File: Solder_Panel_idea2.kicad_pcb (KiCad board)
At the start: 2 copper layers, 152.5 x 101.5 mm, 45 parts, among them SW1 SW_SPDT_1825232-1, U1 SA555P, U2 SA555P

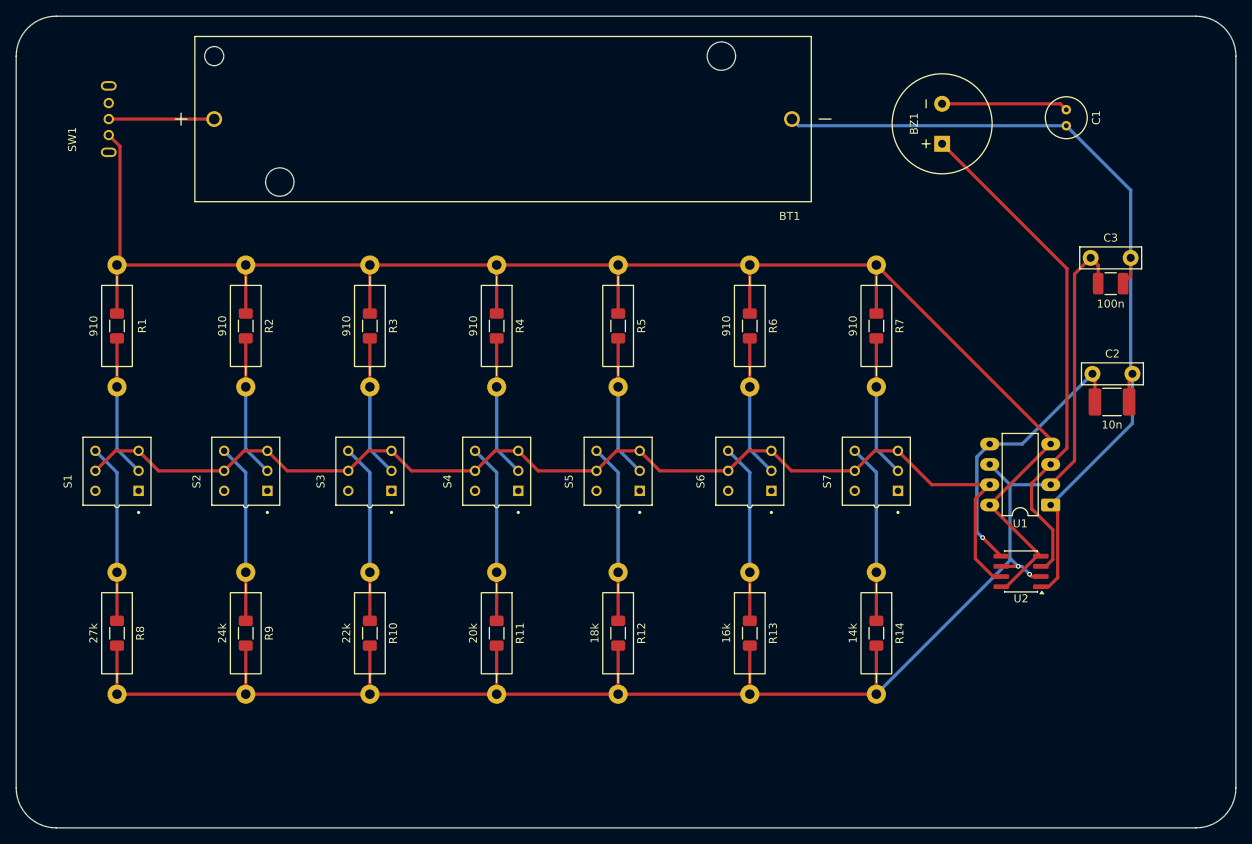
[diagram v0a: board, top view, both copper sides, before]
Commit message: layout changes, art, add 8th note
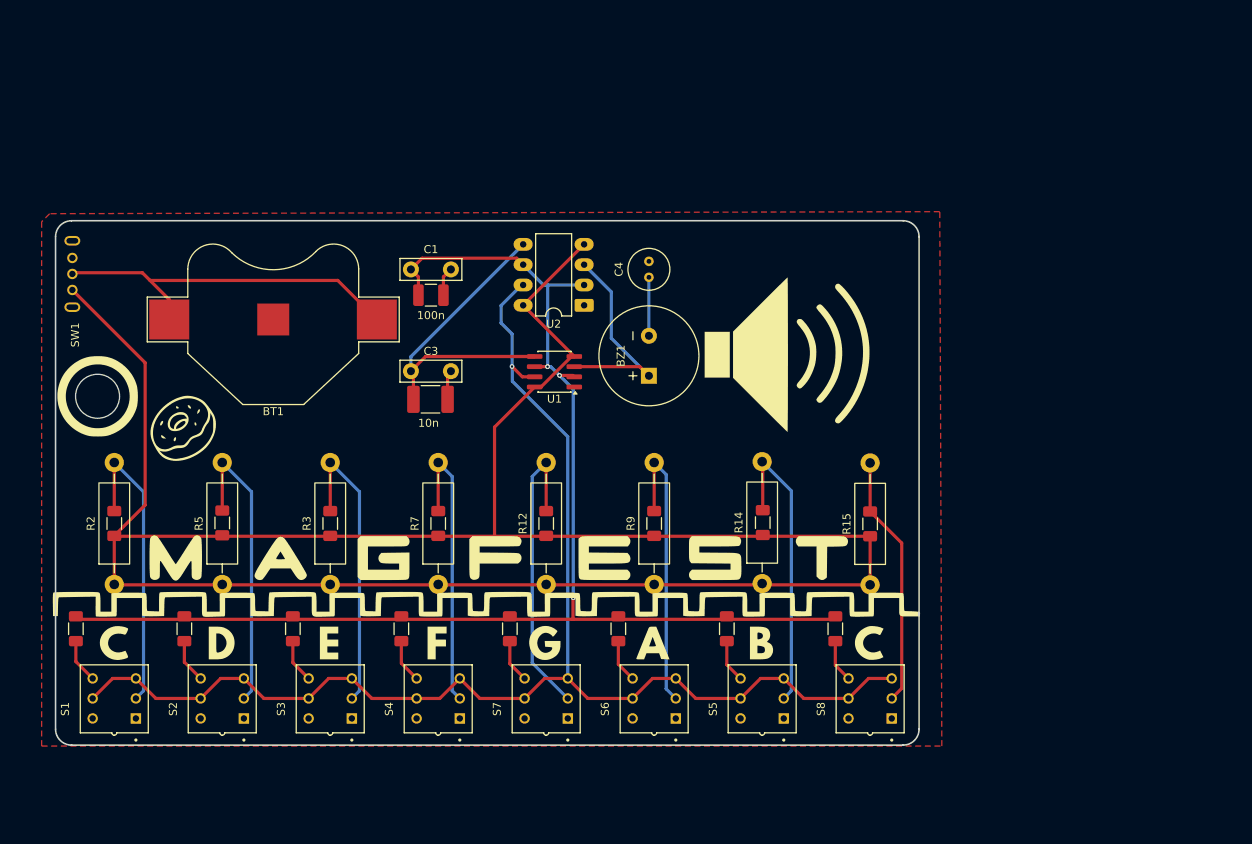
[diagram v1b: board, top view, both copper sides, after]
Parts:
- removed the R13 at (108.5, 85.2)
- removed the R16 at (45.5, 54.4)
- removed the R17 at (61.0, 54.4)
- removed the R18 at (76.9, 54.4)
- removed the R19 at (92.1, 54.4)
- removed the R20 at (108.5, 54.4)
- removed the R21 at (124.3, 54.4)
- added R13: 910, Resistor_SMD:R_1206_3216Metric_Pad1.30x1.75mm_HandSolder, F.Cu at (110.1, 79.0)
- added R13: 910, Resistor_SMD:R_1206_3216Metric_Pad1.30x1.75mm_HandSolder, F.Cu at (123.6, 79.1)
- added R22: 13.2k, Resistor_SMD:R_1206_3216Metric_Pad1.30x1.75mm_HandSolder, F.Cu at (119.2, 92.2)
- added REF**: MountingHole_5.5mm, MountingHole:MountingHole_5.5mm, F.Cu at (27.0, 63.2)
- added S8: C5379898, TL2201EEYA:SW_TL2201EEYA, F.Cu at (123.6, 101.0)
- BT1: footprint 1043:BAT_1043 -> Battery:BatteryHolder_Multicomp_BC-2001_1x2032
- R1, R4, R6: footprint Resistor_THT:R_Axial_DIN0411_L9.9mm_D3.6mm_P15.24mm_Horizontal -> Resistor_SMD:R_1206_3216Metric_Pad1.30x1.75mm_HandSolder
- R10: value 22k -> 910; footprint Resistor_THT:R_Axial_DIN0411_L9.9mm_D3.6mm_P15.24mm_Horizontal -> Resistor_SMD:R_1206_3216Metric_Pad1.30x1.75mm_HandSolder
- R11: value 20k -> 910; footprint Resistor_THT:R_Axial_DIN0411_L9.9mm_D3.6mm_P15.24mm_Horizontal -> Resistor_SMD:R_1206_3216Metric_Pad1.30x1.75mm_HandSolder
- R12: value 18k -> 910
- R14: value 14k -> 910
- R15: footprint Resistor_SMD:R_1206_3216Metric_Pad1.30x1.75mm_HandSolder -> Resistor_THT:R_Axial_DIN0411_L9.9mm_D3.6mm_P15.24mm_Horizontal
- R8: value 27k -> 910; footprint Resistor_THT:R_Axial_DIN0411_L9.9mm_D3.6mm_P15.24mm_Horizontal -> Resistor_SMD:R_1206_3216Metric_Pad1.30x1.75mm_HandSolder
- R9: value 24k -> 910
- S1, S2, S3, S4, S6: value TL2201EEYA -> C5379898; footprint TL2201EEYA:SW_TL2201EEYA -> sao:SW_5.8WSPT
- S5: renamed from S7; value TL2201EEYA -> C5379898
- S7: renamed from S5; value TL2201EEYA -> C5379898; footprint TL2201EEYA:SW_TL2201EEYA -> sao:SW_5.8WSPT
- U1: renamed from U2; value SA555P -> ICM7555IBAZ-T
- U2: renamed from U1; value SA555P -> ICM7555IBAZ-T
- moved R15 99.5 mm to (123.6, 86.8), turned to 90 degrees
- moved C5 85.2 mm to (68.6, 63.6)
- moved C3 85.2 mm to (66.2, 60.0)
- moved C1 85.0 mm to (66.2, 47.3)
- moved C2 85.0 mm to (68.7, 50.5)
- moved R7 67.8 mm to (69.6, 86.7), turned to 90 degrees
- moved R5 63.6 mm to (42.6, 86.7), turned to 90 degrees
- moved U1 63.4 mm to (84.1, 60.1)
- moved U2 63.4 mm to (87.8, 51.8)
- moved R6 61.6 mm to (56.1, 79.1), turned to 90 degrees
- moved C4 56.2 mm to (95.9, 48.3), turned to 90 degrees
- moved R9 51.1 mm to (96.6, 86.7), turned to 90 degrees
- moved R4 47.1 mm to (42.6, 79.0), turned to 90 degrees
- moved BZ1 46.7 mm to (95.9, 58.1)
- moved R2 43.2 mm to (29.1, 86.7), turned to 90 degrees
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- renumbered C3 to C1, C5 to C2, C2 to C3, C1 to C4, C4 to C5, R22 to R15, R24 to R16, R23 to R17, R26 to R18, R25 to R19, R27 to R20, R28 to R21
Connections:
- R10 pad 1: Net-(R10-Pad1) -> Net-(SW1-C)
- R10 pad 2: Net-(U1-THR) -> Net-(R20-Pad2)
- R11 pad 1: Net-(R11-Pad1) -> Net-(SW1-C)
- R11 pad 2: Net-(U1-THR) -> Net-(R19-Pad2)
- R12 pad 1: Net-(R12-Pad1) -> Net-(SW1-C)
- R12 pad 2: Net-(U1-THR) -> Net-(R19-Pad2)
- R14 pad 1: Net-(R14-Pad1) -> Net-(SW1-C)
- R14 pad 2: Net-(U1-THR) -> Net-(R21-Pad2)
- R15 pad 2: Net-(R1-Pad2) -> (no net)
- R2 pad 2: Net-(R16-Pad2) -> Net-(R1-Pad2)
- R4 pad 2: Net-(R18-Pad2) -> Net-(R16-Pad2)
- R5 pad 2: Net-(R19-Pad2) -> Net-(R16-Pad2)
- R6 pad 2: Net-(R20-Pad2) -> Net-(R17-Pad2)
- R7 pad 2: Net-(R21-Pad2) -> Net-(R18-Pad2)
- R8 pad 1: Net-(R22-Pad1) -> Net-(SW1-C)
- R8 pad 2: Net-(U1-THR) -> Net-(R18-Pad2)
- R9 pad 1: Net-(R23-Pad1) -> Net-(SW1-C)
- R9 pad 2: Net-(U1-THR) -> Net-(R20-Pad2)
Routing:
- net GND: track 109.0 -> 7.61 mm
- net Net-(SW1-C): track 212.1 -> 284.3 mm
- net Net-(U1-THR): track 220.1 -> 170.0 mm, vias 2 -> 3
- net (no net): track 0.00 -> 36.9 mm
- net Net-(BZ1--): track 63.2 -> 27.0 mm
- net Net-(SW1-B): track 13.2 -> 46.4 mm
- net Net-(U1-DIS): track 141.2 -> 172.7 mm, vias 0 -> 1
- net Net-(R19-Pad2): track 17.7 -> 38.1 mm
- net Net-(R21-Pad2): track 17.7 -> 37.6 mm
- net Net-(R17-Pad2): track 17.7 -> 37.5 mm
- net Net-(R1-Pad2): track 17.7 -> 37.5 mm
- net Net-(R16-Pad2): track 17.7 -> 37.4 mm
- net Net-(R20-Pad2): track 17.7 -> 36.7 mm
- net Net-(R18-Pad2): track 17.7 -> 36.7 mm
- net Net-(R14-Pad1): track 22.4 -> 5.37 mm
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- added copper zone on F.Cu, net GND
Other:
- board size 152.5 x 101.5 mm -> 107.9 x 65.5 mm
- board text added: "CIRCUITBOARDS@MAGFEST.ORG TEACHING BOARD BUILT BY THE SWADGE TEAM REV 1.0 12.8.2025"
- board text added: "Not a real card. Don't even try it."
- board text added: "Not transferable. Made by your own hands!"
- board text added: "SOLDERING TIPS: 1. HEAT THE JOINT, THEN ADD SOLDER 2. REMOVE THE SOLDER BEFORE THE IRON 3. YOU ONLY NEED A LITTLE BIT OF SOLDER! 4. A GOOD SOLDERED JOINT LOOKS LIKE A TEARDROP ON THE BOARD"
- board text added: "Valid through: 04/20"

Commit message: Update Solder_Panel_idea2.kicad_pcb
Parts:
- S7: renamed from S5; footprint TL2201EEYA:SW_TL2201EEYA -> sao:SW_5.8WSPT
- S8: footprint TL2201EEYA:SW_TL2201EEYA -> sao:SW_5.8WSPT
- renumbered C3 to C1, C1 to C3, R12 to R10, R9 to R11, R13 to R12, R10 to R13, R13 to R15, R15 to R16, R15 to R18, R16 to R19, R18 to R20, R19 to R21, R20 to R22, R21 to R23, R22 to R24, R6 to R3, R3 to R4, R4 to R5, R5 to R6, R8 to R7, R11 to R8, R7 to R9, S3 to S2, S2 to S3, S7 to S4, S4 to S5
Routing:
- net Net-(R18-Pad2): track 36.7 -> 38.9 mm
- net Net-(R21-Pad2): track 37.6 -> 39.2 mm
- net Net-(U1-DIS): track 172.7 -> 171.6 mm
- net Net-(R16-Pad2): track 37.4 -> 38.3 mm
- net Net-(R1-Pad2): track 37.5 -> 38.4 mm
- net Net-(R17-Pad2): track 37.5 -> 38.4 mm
- net Net-(R20-Pad2): track 36.7 -> 37.3 mm
